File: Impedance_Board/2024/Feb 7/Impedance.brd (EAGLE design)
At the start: 70 x 70 mm, 47 parts, among them U2 INA826AID, U3 MC74VHC1GT66DTT1, U4 MC74VHC1GT66DTT1, U7 AD8606ARZ, U8 AD8606ARZ

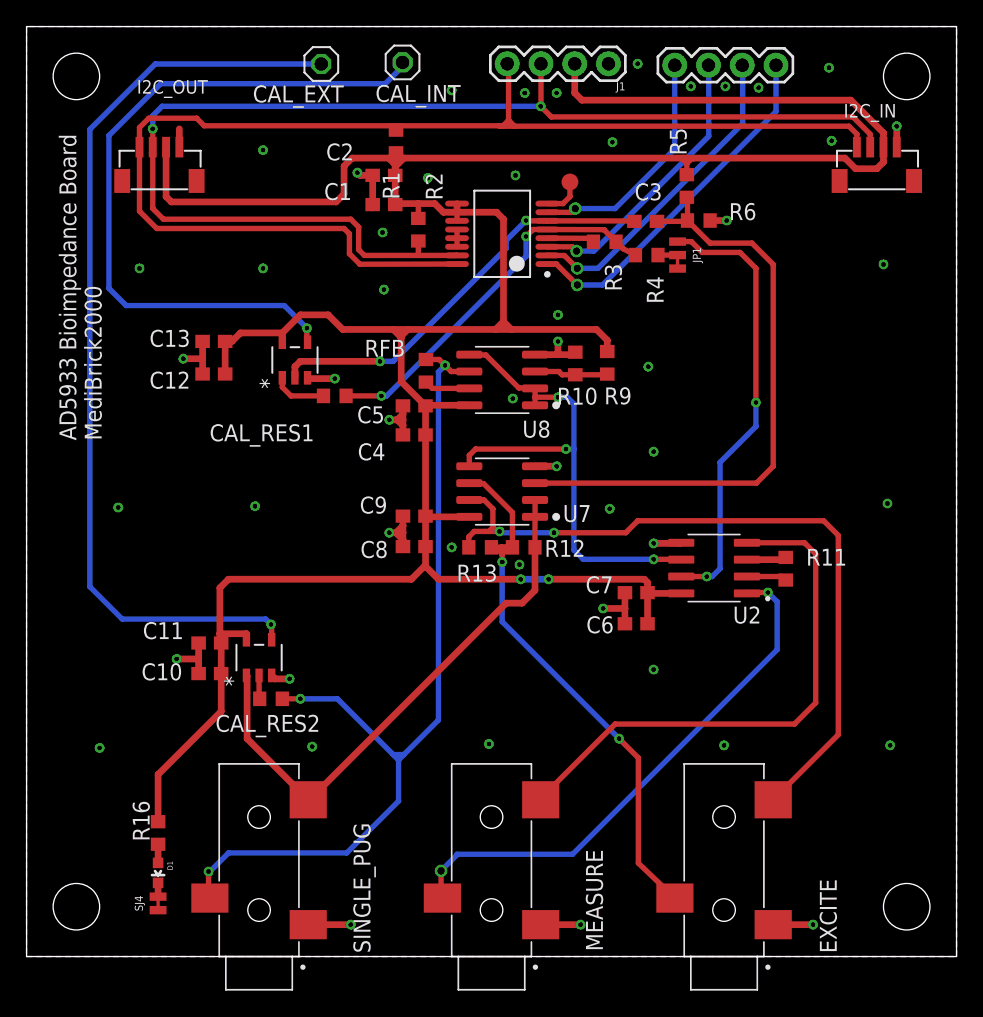
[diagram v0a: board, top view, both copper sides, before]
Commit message: Updated SPO2
Crosse Checked with Data Sheet and Evaluation Board
Added 10Ohm resistors in data lines
Adjusted capacitors
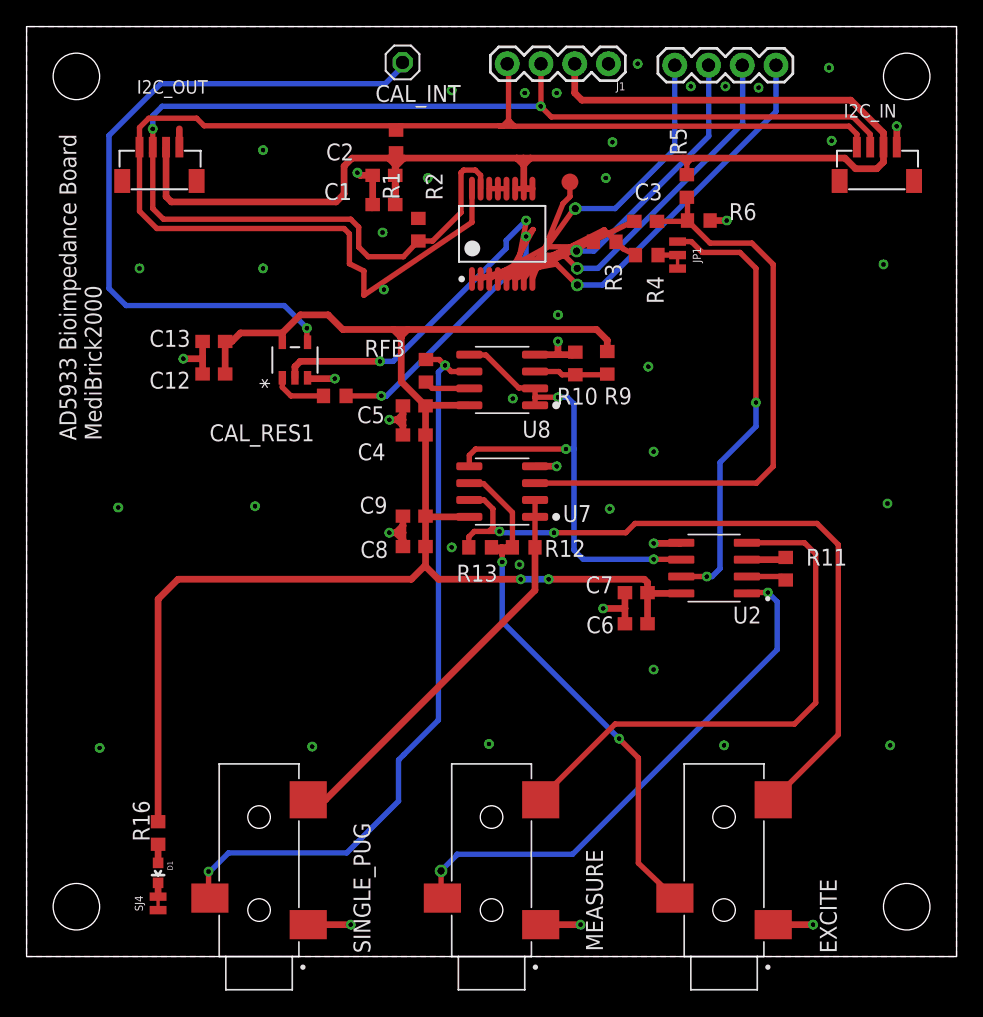
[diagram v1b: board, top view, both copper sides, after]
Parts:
- removed C10: 0.1uF, rcl:C0603
- removed C11: 10uF, rcl:C0603
- removed CAL_EXT: (no value), pinhead:1X01
- removed CAL_RES2: 2K, rcl:R0603
- removed U3: MC74VHC1GT66DTT1, MC74VHC1GT66DTT1:TSOP5_1P65X3P15_ONS
- turned AD5933 to 90 degrees
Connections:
- removed net N$22: CAL_RES2.2, U3.2
- removed net N$27: CAL_EXT.1, U3.4
- net 3.3V: no longer C10.1, C11.1, U3.5
- net GND: no longer C10.2, C11.2, U3.3
- net N$15: no longer U3.1
- net N$17: no longer CAL_RES2.1
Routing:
- net N$27: track 69.9 -> 0.00 mm, vias 1 -> 0
- net 3.3V: track 241.3 -> 226.8 mm
- net N$17: track 68.1 -> 56.6 mm, vias 3 -> 2
- net N$15: track 41.7 -> 30.4 mm
- net SCL: track 94.7 -> 102.5 mm
- net VIN: track 28.6 -> 35.7 mm
- net VOUT: track 31.3 -> 37.6 mm
- net SDA: track 93.1 -> 99.3 mm
- net N$3: track 26.8 -> 32.5 mm
- net GND: track 51.6 -> 46.0 mm, vias 50 -> 48
- net N$4: track 24.0 -> 29.3 mm
- net N$10: track 21.2 -> 26.2 mm
- net MCLK: track 3.02 -> 7.97 mm
- net N$5: track 3.60 -> 7.96 mm
- net N$11: track 17.9 -> 22.2 mm
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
